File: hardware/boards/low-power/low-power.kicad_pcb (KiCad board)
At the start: 2 copper layers, 82.1 x 77.1 mm, 127 parts, among them J1 Conn_01x05_Pin, J2 Conn_01x32_Pin, J3 U.FL, J4 U.FL, J5 USB_C_Receptacle_USB2.0, J6 Conn_01x03_Pin, Q1 DMN2400UFB4, U1 L80-R, U10 IS31FL3197, U11 AP63356QZV-7, U12 AP63356QZV-7, U13 INA2180A3IDSGR, U14 CYPD3177, U2 TX5813, U3 SX1262IMLTRT, U4 SKY13453-385LF, U5 W25Q128JVPIQ, U6 RP2040, U7 TCA9539RTWR, U8 TMUX1309BQBR, U9 LSM6DSM, Y1 32 MHz, Y2 12 MHz

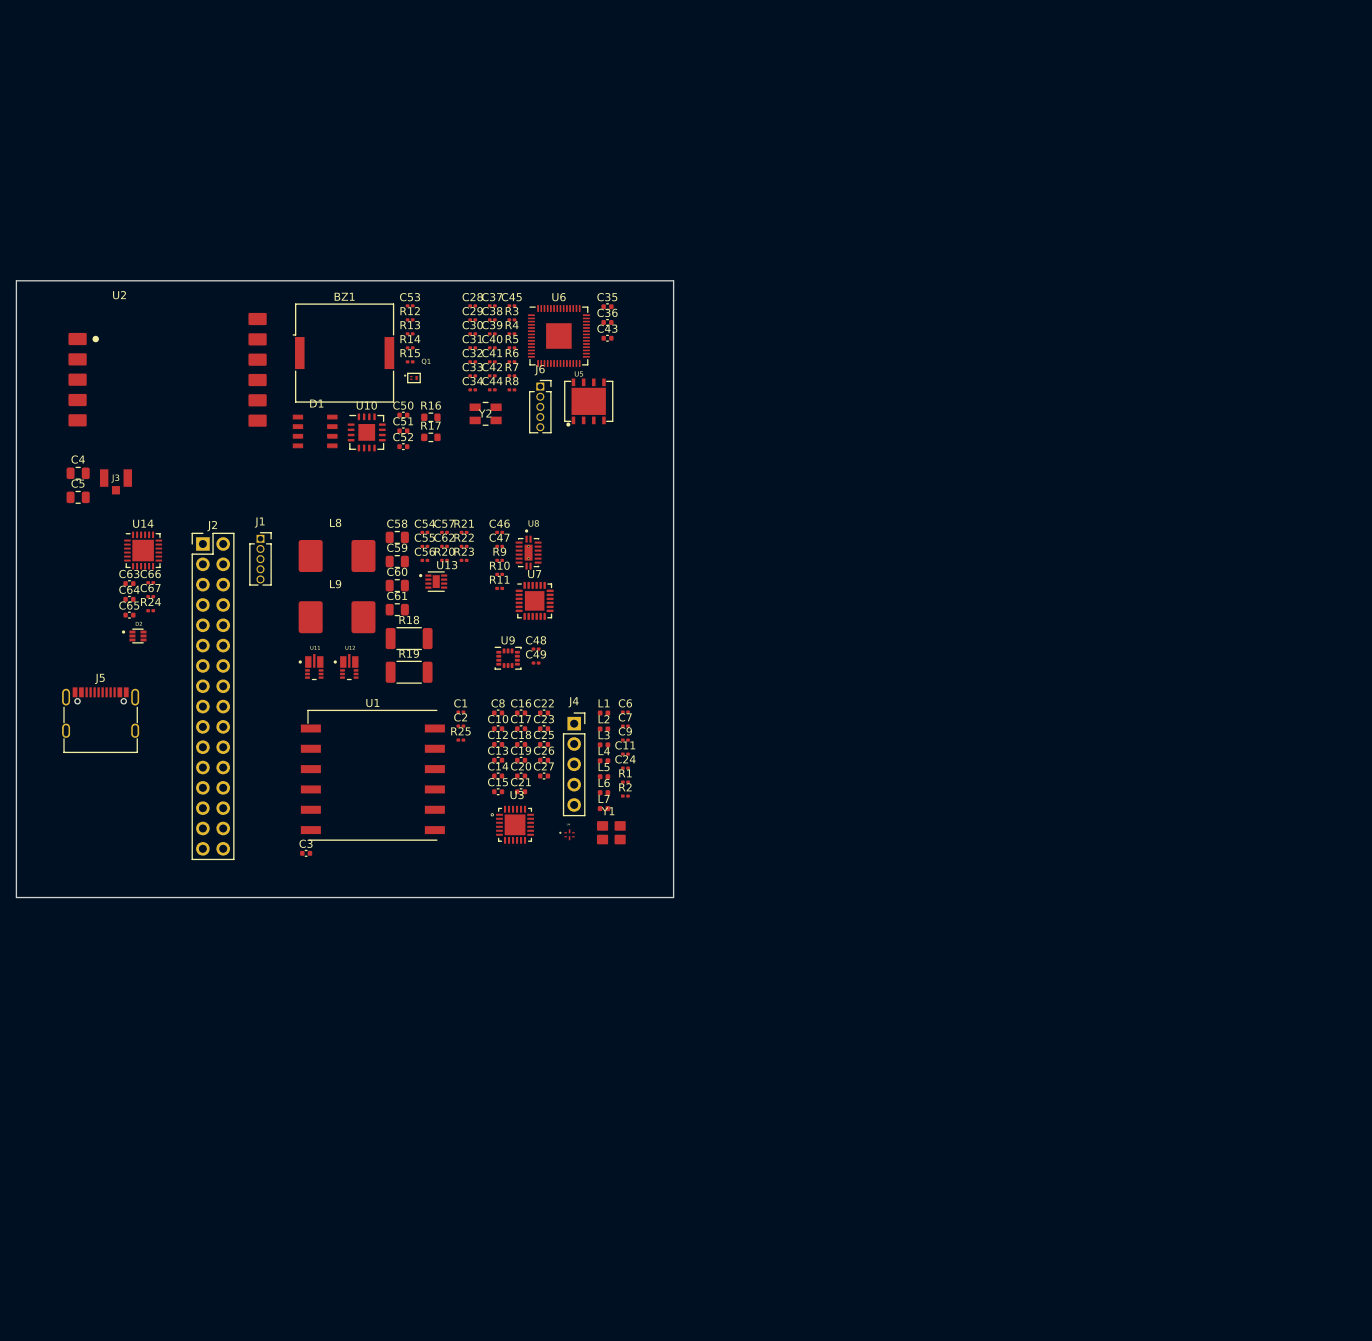
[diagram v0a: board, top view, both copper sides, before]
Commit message: Add footprints and models for LP board
Also completed rough layout for LP board to estimate board space usage.
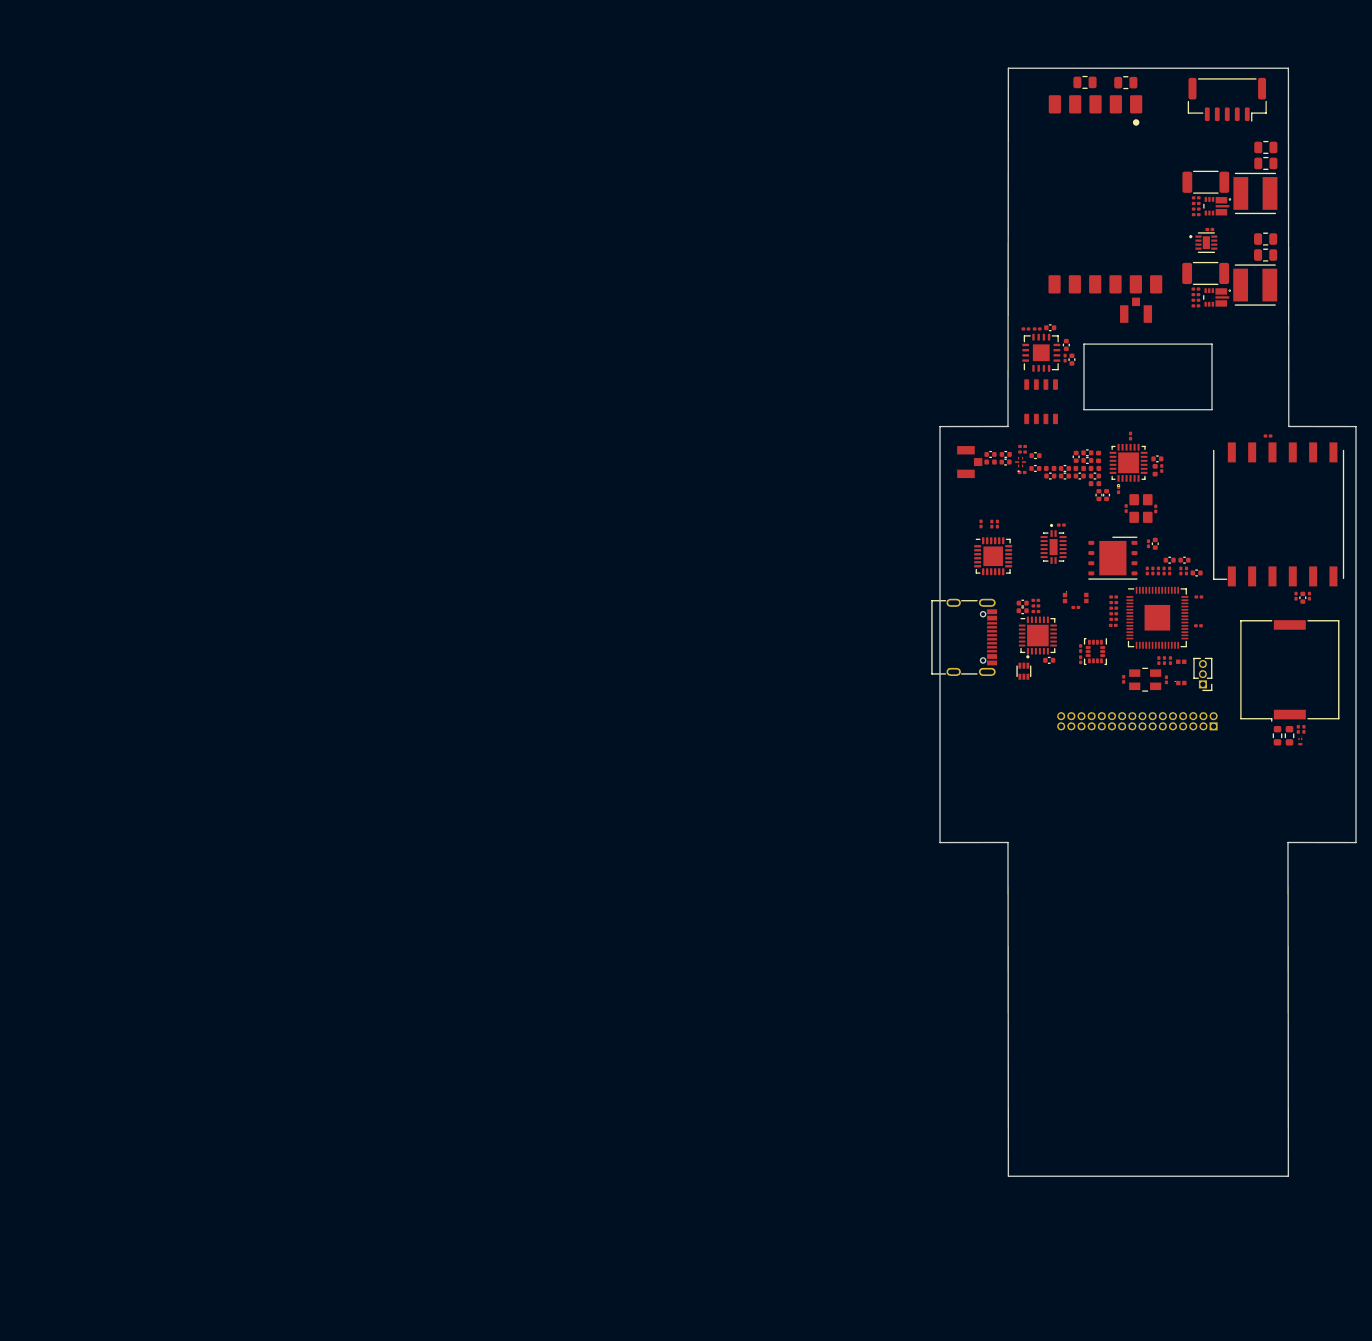
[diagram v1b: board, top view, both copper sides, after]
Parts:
- added C68: 100n, Capacitor_SMD:C_0201_0603Metric, F.Cu at (213.8, 83.0)
- added SW1: SW_Push, capstone:R-668048, F.Cu at (217.4, 95.6)
- added SW2: SW_Push, capstone:R-668048, F.Cu at (204.2, 86.3)
- BZ1: footprint Buzzer_Beeper:Buzzer_Murata_PKLCS1212E -> capstone:Buzzer_Murata_PKLCS1212E
- C23: footprint Capacitor_SMD:C_0402_1005Metric -> Capacitor_SMD:C_0201_0603Metric
- C28: footprint Capacitor_SMD:C_0201_0603Metric -> Capacitor_SMD:C_0402_1005Metric
- J1: footprint Connector_PinSocket_1.27mm:PinSocket_1x05_P1.27mm_Vertical -> Connector_JST:JST_GH_SM05B-GHS-TB_1x05-1MP_P1.25mm_Horizontal
- J2: footprint Connector_PinHeader_2.54mm:PinHeader_2x16_P2.54mm_Vertical -> Connector_PinHeader_1.27mm:PinHeader_2x16_P1.27mm_Vertical; moved to B.Cu
- J4: footprint Connector_PinSocket_2.54mm:PinSocket_1x05_P2.54mm_Vertical -> capstone:U.FL-R-SMT-1(60)
- J6: footprint Connector_PinSocket_1.27mm:PinSocket_1x05_P1.27mm_Vertical -> Connector_PinHeader_1.27mm:PinHeader_1x03_P1.27mm_Vertical
- L8, L9: footprint capstone:MHCB06030 -> capstone:IND_LQH5BPN6R8NT0L
- U1: footprint RF_GPS:Quectel_L80-R -> capstone:Quectel_L80-R
- U5: footprint capstone:SON127P610X510X80-8N430X340 -> Package_SON:WSON-8-1EP_6x5mm_P1.27mm_EP3.4x4.3mm
- moved C4 139.8 mm to (210.5, 21.9), turned to 180 degrees
- moved C5 136.1 mm to (205.4, 21.9)
- moved J1 132.7 mm to (223.2, 24.0), turned to 180 degrees
- moved J3 129.1 mm to (211.7, 50.8), turned to 180 degrees
- moved C3 128.6 mm to (232.6, 86.3), turned to -90 degrees
- moved J2 128.4 mm to (221.4, 102.4), turned to 90 degrees
- moved U11 126.6 mm to (221.7, 37.4), turned to -90 degrees
- moved BZ1 124.6 mm to (231.0, 95.3), turned to 90 degrees
- moved L8 123.4 mm to (226.7, 35.8)
- moved U2 122.1 mm to (202.3, 30.0), turned to -90 degrees
- moved L9 122.0 mm to (226.6, 47.2)
- moved C60 121.6 mm to (228.0, 30.0), turned to 180 degrees
- moved R14 120.8 mm to (232.0, 102.8), turned to -90 degrees
- moved R15 120.8 mm to (232.7, 102.8), turned to -90 degrees
- moved Q1 119.8 mm to (232.3, 104.3), turned to -90 degrees
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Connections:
- U10 pad 17: (no net) -> GND
- U7 pad 25: (no net) -> GND
- U9 pad 7: (no net) -> GND
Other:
- board size 82.1 x 77.1 mm -> 52 x 138.5 mm

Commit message: Add initial changes after schematic review
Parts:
- moved J1 145.7 mm to (155.4, 153.0), turned to -90 degrees
- moved C60 134.5 mm to (157.9, 144.8), turned to -90 degrees
- moved C58 131.7 mm to (159.9, 144.8), turned to -90 degrees
- moved R18 131.5 mm to (162.3, 152.3), turned to 90 degrees
- moved R21 129.5 mm to (164.2, 153.5), turned to -90 degrees
- moved C55 128.6 mm to (164.9, 153.5), turned to 90 degrees
- moved R20 127.6 mm to (165.6, 153.5), turned to 90 degrees
- moved L8 127.1 mm to (163.7, 146.1), turned to 90 degrees
- moved U11 126.9 mm to (165.3, 151.1), turned to 0 degrees
- moved C54 126.7 mm to (166.3, 153.5), turned to -90 degrees
- moved C62 123.4 mm to (168.2, 151.8), turned to -90 degrees
- moved U13 121.4 mm to (169.8, 152.3), turned to 90 degrees
- moved C61 118.8 mm to (169.4, 144.8), turned to -90 degrees
- moved R19 116.4 mm to (173.7, 152.3), turned to 90 degrees
- moved C59 116.1 mm to (171.4, 144.8), turned to -90 degrees
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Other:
- board size 52 x 138.5 mm -> 110.8 x 163.5 mm
